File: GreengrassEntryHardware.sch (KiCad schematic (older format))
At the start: 29 parts

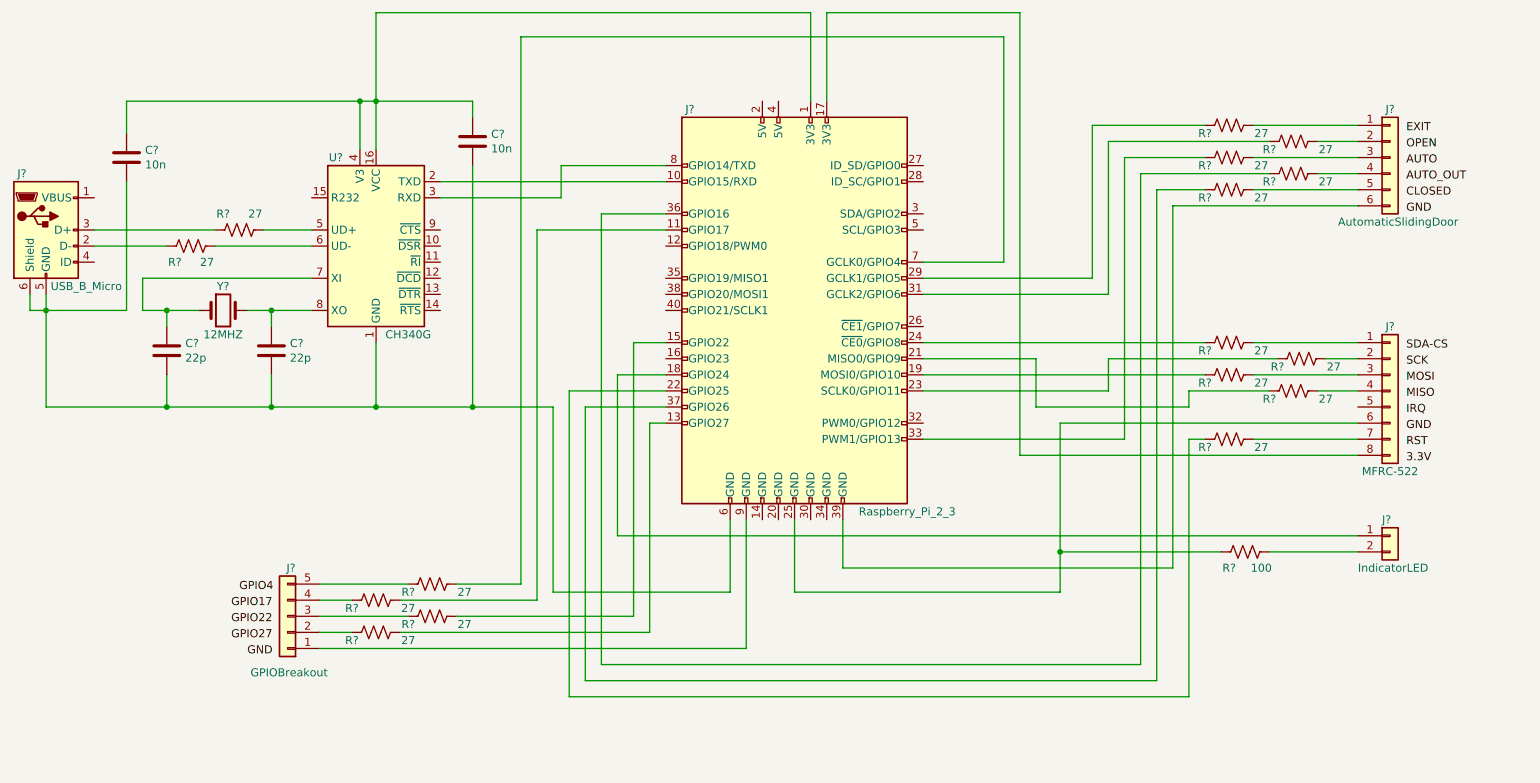
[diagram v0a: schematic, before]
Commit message: WIP: finished usb to uart design
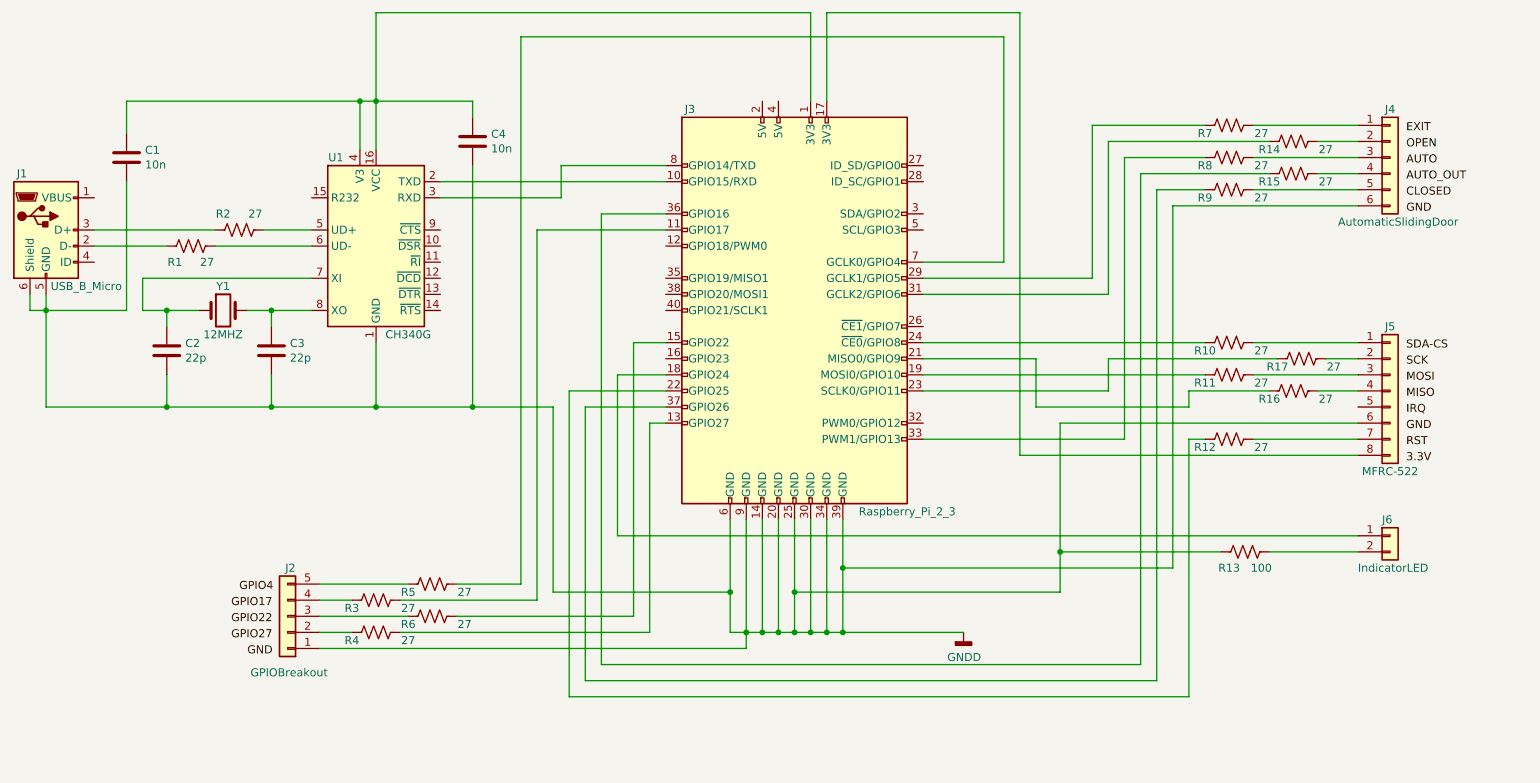
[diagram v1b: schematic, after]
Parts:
- C1, C2, C3, C4: renamed from C?; footprint (none) -> Capacitor_SMD:C_0805_2012Metric_Pad1.15x1.40mm_HandSolder
- J1: renamed from J?; footprint (none) -> GreengrassEntryHardware:MicroUSB
- J2: renamed from J?; footprint (none) -> Connector_PinHeader_2.54mm:PinHeader_1x05_P2.54mm_Vertical
- J3: renamed from J?; footprint (none) -> Connector_PinSocket_2.54mm:PinSocket_2x20_P2.54mm_Vertical
- J4: renamed from J?; footprint (none) -> Connector_PinHeader_2.54mm:PinHeader_1x06_P2.54mm_Vertical
- J5: renamed from J?; footprint (none) -> Connector_PinHeader_2.54mm:PinHeader_1x08_P2.54mm_Vertical
- J6: renamed from J?; footprint (none) -> Connector_PinHeader_2.54mm:PinHeader_2x01_P2.54mm_Horizontal
- R1, R10, R11, R12, R13, R14, R15, R16, R17, R2, R3, R4, R5, R6, R7, R8, R9: renamed from R?; footprint (none) -> Resistor_SMD:R_0805_2012Metric_Pad1.15x1.40mm_HandSolder
- Y1: renamed from Y?; footprint (none) -> Crystal:Crystal_SMD_HC49-SD_HandSoldering
- gave numbers to parts that had none: 1
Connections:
- net GNDD: now reaches J3.14 (GND)
- net GNDD: now also C1.2, C2.2, C3.2, C4.2, J1.5 (GND), J1.6 (Shield), J2.1 (Pin_1), J3.20 (GND), J3.25 (GND), J3.30 (GND), J3.34 (GND), J3.39 (GND), J3.6 (GND), J3.9 (GND), J4.6 (Pin_6), J5.6 (Pin_6), R13.2, U1.1 (GND)

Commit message: Added GPIO breakout to pcb
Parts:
- J2: footprint Connector_PinHeader_2.54mm:PinHeader_1x05_P2.54mm_Vertical -> Connector_PinHeader_2.54mm:PinHeader_1x05_P2.54mm_Horizontal
- renumbered R4 to R3, R6 to R4, R3 to R5, R5 to R6
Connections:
- net at J3.11 (GPIO17): now also R4.1; no longer R5.1
- net at J3.13 (GPIO27): now also R5.1; no longer R3.1
- net at J3.15 (GPIO22): now also R6.1; no longer R4.1
- net at J3.7 (GCLK0/GPIO4): now also R3.1; no longer R6.1
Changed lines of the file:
@@
 Wire Wire Line
 	3300 4450 3900 4450
-Wire Wire Line
-	4400 5600 5500 5600
-Wire Wire Line
-	5500 5600 5500 5150
 Connection ~ 3300 4450
 $Comp
@@
 F 0 "J2" H 2700 5450 50  0000 L CNN
 F 1 "GPIOBreakout" H 2500 6100 50  0000 L CNN
-F 2 "Connector_PinHeader_2.54mm:PinHeader_1x05_P2.54mm_Vertical" H 2750 5750 50  0001 C CNN
+F 2 "Connector_PinHeader_2.54mm:PinHeader_1x05_P2.54mm_Horizontal" H 2750 5750 50  0001 C CNN
 F 3 "~" H 2750 5750 50  0001 C CNN
 	1    2750 5750
@@
 Text Label 2500 6000 0    50   ~ 0
 GND
-Text Label 2450 5600 0    50   ~ 0
+Text Label 2450 5900 0    50   ~ 0
 GPIO4
+Text Label 2400 5800 0    50   ~ 0
+GPIO17
 Text Label 2400 5700 0    50   ~ 0
-GPIO17
-Text Label 2400 5900 0    50   ~ 0
 GPIO27
-Text Label 2400 5800 0    50   ~ 0
-GPIO22
 Wire Wire Line
 	5600 5150 5600 5850
 Wire Wire Line
-	3800 5750 4900 5750
-Wire Wire Line
-	4900 5750 4900 4050
-Wire Wire Line
 	4900 4050 5100 4050
 Wire Wire Line
-	5000 5850 5000 4550
-Wire Wire Line
 	5000 4550 5100 4550
 Wire Wire Line
-	4300 5650 4300 3350
-Wire Wire Line
 	4300 3350 5100 3350
 Wire Wire Line
-	3800 5550 4200 5550
-Wire Wire Line
-	4200 5550 4200 2150
-Wire Wire Line
 	7200 2150 7200 3550
 Wire Wire Line
@@
 	4200 2150 7200 2150
 $Comp
-L Device:R_US R5
-U 1 1 5D518DBE
-P 3650 5550
-F 0 "R5" V 3700 5400 50  0000 C CNN
-F 1 "27" V 3700 5750 50  0000 C CNN
-F 2 "Resistor_SMD:R_0805_2012Metric_Pad1.15x1.40mm_HandSolder" V 3690 5540 50  0001 C CNN
-F 3 "~" H 3650 5550 50  0001 C CNN
-	1    3650 5550
-	0    1    1    0
-$EndComp
-$Comp
-L Device:R_US R6
-U 1 1 5D5193C5
-P 3650 5750
-F 0 "R6" V 3700 5600 50  0000 C CNN
-F 1 "27" V 3700 5950 50  0000 C CNN
-F 2 "Resistor_SMD:R_0805_2012Metric_Pad1.15x1.40mm_HandSolder" V 3690 5740 50  0001 C CNN
-F 3 "~" H 3650 5750 50  0001 C CNN
-	1    3650 5750
-	0    1    1    0
-$EndComp
-$Comp
-L Device:R_US R4
+L Device:R_US R3
 U 1 1 5D519DE6
 P 3300 5850
-F 0 "R4" V 3350 5700 50  0000 C CNN
+F 0 "R3" V 3350 5700 50  0000 C CNN
 F 1 "27" V 3350 6050 50  0000 C CNN
 F 2 "Resistor_SMD:R_0805_2012Metric_Pad1.15x1.40mm_HandSolder" V 3340 5840 50  0001 C CNN
@@
 	0    1    1    0
 $EndComp
-$Comp
-L Device:R_US R3
-U 1 1 5D51ABA1
-P 3300 5650
-F 0 "R3" V 3350 5500 50  0000 C CNN
-F 1 "27" V 3350 5850 50  0000 C CNN
-F 2 "Resistor_SMD:R_0805_2012Metric_Pad1.15x1.40mm_HandSolder" V 3340 5640 50  0001 C CNN
-F 3 "~" H 3300 5650 50  0001 C CNN
-	1    3300 5650
-	0    1    1    0
-$EndComp
-Wire Wire Line
-	2950 5550 3500 5550
 Wire Wire Line
 	2950 5650 3150 5650
@@
 	2950 5850 3150 5850
 Wire Wire Line
-	2950 5950 5600 5950
-Wire Wire Line
-	3450 5850 5000 5850
-Wire Wire Line
-	3450 5650 4300 5650
-Wire Wire Line
 	4800 5250 4800 4250
 Wire Wire Line
@@
 	3700 3050 5100 3050
 Wire Wire Line
-	4400 4450 4400 5600
+	4400 4450 4400 5350
 Wire Wire Line
 	8450 4650 8350 4650
@@
 	9400 5250 4800 5250
 $Comp
-L power:GNDD #PWR?
+L power:GNDD #PWR0101
 U 1 1 5D3B21CF
 P 6950 5850
-F 0 "#PWR?" H 6950 5600 50  0001 C CNN
+F 0 "#PWR0101" H 6950 5600 50  0001 C CNN
 F 1 "GNDD" H 6954 5695 50  0000 C CNN
 F 2 "" H 6950 5850 50  0001 C CNN
@@
 	5600 5850 5600 5950
 Wire Wire Line
-	5500 5600 5500 5850
-Wire Wire Line
 	5500 5850 5600 5850
-Connection ~ 5500 5600
+Wire Wire Line
+	5500 5150 5500 5350
+Wire Wire Line
+	5500 5350 4400 5350
+Connection ~ 5500 5350
+Wire Wire Line
+	5000 4550 5000 5650
+Wire Wire Line
+	4900 4050 4900 5550
+Wire Wire Line
+	4300 3350 4300 5750
+Wire Wire Line
+	5500 5350 5500 5850
+Wire Wire Line
+	2950 5550 3500 5550
+Wire Wire Line
+	3450 5850 4200 5850
+Wire Wire Line
+	4200 2150 4200 5850
+Wire Wire Line
+	3800 5750 4300 5750
+Wire Wire Line
+	2950 5950 5600 5950
+Wire Wire Line
+	3450 5650 5000 5650
+Wire Wire Line
+	3800 5550 4900 5550
+$Comp
+L Device:R_US R6
+U 1 1 5D518DBE
+P 3650 5550
+F 0 "R6" V 3700 5400 50  0000 C CNN
+F 1 "27" V 3700 5750 50  0000 C CNN
+F 2 "Resistor_SMD:R_0805_2012Metric_Pad1.15x1.40mm_HandSolder" V 3690 5540 50  0001 C CNN
+F 3 "~" H 3650 5550 50  0001 C CNN
+	1    3650 5550
+	0    1    1    0
+$EndComp
+$Comp
+L Device:R_US R5
+U 1 1 5D51ABA1
+P 3300 5650
+F 0 "R5" V 3350 5500 50  0000 C CNN
+F 1 "27" V 3350 5850 50  0000 C CNN
+F 2 "Resistor_SMD:R_0805_2012Metric_Pad1.15x1.40mm_HandSolder" V 3340 5640 50  0001 C CNN
+F 3 "~" H 3300 5650 50  0001 C CNN
+	1    3300 5650
+	0    1    1    0
+$EndComp
+$Comp
+L Device:R_US R4
+U 1 1 5D5193C5
+P 3650 5750
+F 0 "R4" V 3700 5600 50  0000 C CNN
+F 1 "27" V 3700 5950 50  0000 C CNN
+F 2 "Resistor_SMD:R_0805_2012Metric_Pad1.15x1.40mm_HandSolder" V 3690 5740 50  0001 C CNN
+F 3 "~" H 3650 5750 50  0001 C CNN
+	1    3650 5750
+	0    1    1    0
+$EndComp
+Text Label 2400 5600 0    50   ~ 0
+GPIO22
 $EndSCHEMATC

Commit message: Tidied up the mfrc pcb layout
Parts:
- removed J6: IndicatorLED, Connector_PinHeader_2.54mm:PinHeader_2x01_P2.54mm_Horizontal, symbol Connector_Generic:Conn_01x02
- added R18: 27, Resistor_SMD:R_0805_2012Metric_Pad1.15x1.40mm_HandSolder, symbol Device:R_US
- J5: footprint Connector_PinHeader_2.54mm:PinHeader_1x08_P2.54mm_Vertical -> Connector_PinHeader_2.54mm:PinHeader_2x05_P2.54mm_Horizontal; symbol Connector_Generic:Conn_01x08 -> Connector_Generic:Conn_01x10
- R13: value 100 -> 27
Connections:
- net GNDD: now also J4.1 (Pin_1); no longer J4.6 (Pin_6), R13.2
- net at J3.16 (GPIO23): now also R18.2
- net at J3.18 (GPIO24): now also R13.2
- net at R7.1: now also J4.2 (Pin_2); no longer J4.1 (Pin_1)
- net at R14.1: now also J4.3 (Pin_3); no longer J4.2 (Pin_2)
- net at R8.1: now also J4.4 (Pin_4); no longer J4.3 (Pin_3)
- net at R15.1: now also J4.5 (Pin_5); no longer J4.4 (Pin_4)
- net at R9.1: now also J4.6 (Pin_6); no longer J4.5 (Pin_5)
- net at R13.1: now also J5.9 (Pin_9)
- new net: J5.10 (Pin_10), R18.1
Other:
- moved on the sheet: J4, R17
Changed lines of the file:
@@
 SDA-CS
 $Comp
-L Connector_Generic:Conn_01x08 J5
+L Connector_Generic:Conn_01x10 J5
 U 1 1 5D3BD9C3
-P 9600 4350
-F 0 "J5" H 9600 4750 50  0000 C CNN
+P 9600 4450
+F 0 "J5" H 9600 5000 50  0000 C CNN
 F 1 "MFRC-522" H 9600 3850 50  0000 C CNN
-F 2 "Connector_PinHeader_2.54mm:PinHeader_1x08_P2.54mm_Vertical" H 9600 4350 50  0001 C CNN
-F 3 "~" H 9600 4350 50  0001 C CNN
-	1    9600 4350
+F 2 "Connector_PinHeader_2.54mm:PinHeader_2x05_P2.54mm_Horizontal" H 9600 4450 50  0001 C CNN
+F 3 "~" H 9600 4450 50  0001 C CNN
+	1    9600 4450
 	1    0    0    -1
 $EndComp
@@
 Wire Wire Line
 	4500 4350 4500 6250
-Text Label 9700 3250 0    50   ~ 0
+Text Label 9700 2650 0    50   ~ 0
 GND
 Text Label 9700 3150 0    50   ~ 0
@@
 L Connector_Generic:Conn_01x06 J4
 U 1 1 5D3C1839
-P 9600 2900
-F 0 "J4" H 9600 3200 50  0000 C CNN
-F 1 "AutomaticSlidingDoor" H 9650 2500 50  0000 C CNN
-F 2 "Connector_PinHeader_2.54mm:PinHeader_1x06_P2.54mm_Vertical" H 9600 2900 50  0001 C CNN
-F 3 "~" H 9600 2900 50  0001 C CNN
-	1    9600 2900
+P 9600 2800
+F 0 "J4" H 9600 3100 50  0000 C CNN
+F 1 "AutomaticSlidingDoor" H 9650 2400 50  0000 C CNN
+F 2 "Connector_PinHeader_2.54mm:PinHeader_1x06_P2.54mm_Vertical" H 9600 2800 50  0001 C CNN
+F 3 "~" H 9600 2800 50  0001 C CNN
+	1    9600 2800
 	1    0    0    -1
 $EndComp
@@
 	6100 2000 7300 2000
 Wire Wire Line
-	8250 3200 8250 5450
-Wire Wire Line
 	7550 5600 5900 5600
 Wire Wire Line
 	5900 5600 5900 5150
-Wire Wire Line
-	6200 5150 6200 5450
-Wire Wire Line
-	6200 5450 8250 5450
 Wire Wire Line
 	8450 3100 8150 3100
@@
 	3300 4450 3900 4450
 Connection ~ 3300 4450
-$Comp
-L Connector_Generic:Conn_01x02 J6
-U 1 1 5D44B757
-P 9600 5250
-F 0 "J6" H 9550 5350 50  0000 L CNN
-F 1 "IndicatorLED" H 9400 5050 50  0000 L CNN
-F 2 "Connector_PinHeader_2.54mm:PinHeader_2x01_P2.54mm_Horizontal" H 9600 5250 50  0001 C CNN
-F 3 "~" H 9600 5250 50  0001 C CNN
-	1    9600 5250
-	1    0    0    -1
-$EndComp
 Wire Wire Line
 	4800 4250 5100 4250
@@
 L Device:R_US R17
 U 1 1 5D47C1CF
-P 9050 4150
-F 0 "R17" V 9100 4000 50  0000 C CNN
-F 1 "27" V 9100 4350 50  0000 C CNN
-F 2 "Resistor_SMD:R_0805_2012Metric_Pad1.15x1.40mm_HandSolder" V 9090 4140 50  0001 C CNN
-F 3 "~" H 9050 4150 50  0001 C CNN
-	1    9050 4150
-	0    1    1    0
-$EndComp
-Wire Wire Line
-	8900 4150 7850 4150
+P 9000 4150
+F 0 "R17" V 9050 4000 50  0000 C CNN
+F 1 "27" V 9050 4350 50  0000 C CNN
+F 2 "Resistor_SMD:R_0805_2012Metric_Pad1.15x1.40mm_HandSolder" V 9040 4140 50  0001 C CNN
+F 3 "~" H 9000 4150 50  0001 C CNN
+	1    9000 4150
+	0    1    1    0
+$EndComp
 $Comp
 L Device:R_US R11
@@
 	8750 3100 9400 3100
 Wire Wire Line
-	8250 3200 9400 3200
-Wire Wire Line
 	7850 2800 8850 2800
 Wire Wire Line
@@
 Wire Wire Line
 	8750 4050 9400 4050
-Wire Wire Line
-	9200 4150 9400 4150
 Wire Wire Line
 	8750 4250 9400 4250
@@
 	1150 3850 1250 3850
 $Comp
-L Device:R_US R13
-U 1 1 5D455FFA
-P 8700 5350
-F 0 "R13" V 8800 5250 50  0000 C CNN
-F 1 "100" V 8800 5450 50  0000 C CNN
-F 2 "Resistor_SMD:R_0805_2012Metric_Pad1.15x1.40mm_HandSolder" V 8740 5340 50  0001 C CNN
-F 3 "~" H 8700 5350 50  0001 C CNN
-	1    8700 5350
-	0    1    1    0
-$EndComp
-Wire Wire Line
-	7550 4550 7550 5350
-Wire Wire Line
-	8550 5350 7550 5350
-Connection ~ 7550 5350
-Wire Wire Line
-	7550 5350 7550 5600
-Wire Wire Line
-	8850 5350 9400 5350
-Wire Wire Line
-	9400 5250 4800 5250
-$Comp
 L power:GNDD #PWR0101
 U 1 1 5D3B21CF
@@
 	6950 5850 6200 5850
 Wire Wire Line
-	6200 5850 6200 5450
-Connection ~ 6200 5450
-Wire Wire Line
 	6200 5850 6100 5850
 Wire Wire Line
@@
 	5500 5850 5600 5850
 Wire Wire Line
-	5500 5150 5500 5350
-Wire Wire Line
-	5500 5350 4400 5350
-Connection ~ 5500 5350
-Wire Wire Line
 	5000 4550 5000 5650
 Wire Wire Line
@@
 Wire Wire Line
 	4300 3350 4300 5750
-Wire Wire Line
-	5500 5350 5500 5850
 Wire Wire Line
 	2950 5550 3500 5550
@@
 Text Label 2400 5600 0    50   ~ 0
 GPIO22
+Text Label 9700 4900 0    50   ~ 0
+LED
+$Comp
+L Device:R_US R13
+U 1 1 5D59BAAD
+P 8600 4850
+F 0 "R13" V 8650 4700 50  0000 C CNN
+F 1 "27" V 8650 5050 50  0000 C CNN
+F 2 "Resistor_SMD:R_0805_2012Metric_Pad1.15x1.40mm_HandSolder" V 8640 4840 50  0001 C CNN
+F 3 "~" H 8600 4850 50  0001 C CNN
+	1    8600 4850
+	0    1    1    0
+$EndComp
+Wire Wire Line
+	7950 4850 7950 5250
+Wire Wire Line
+	7950 5250 4800 5250
+Wire Wire Line
+	7550 4550 7550 5600
+Wire Wire Line
+	5500 5350 5500 5850
+Wire Wire Line
+	5500 5150 5500 5350
+Connection ~ 5500 5350
+Wire Wire Line
+	5500 5350 4400 5350
+Wire Wire Line
+	6200 5150 6200 5350
+Wire Wire Line
+	6200 5350 7650 5350
+Connection ~ 6200 5350
+Wire Wire Line
+	6200 5350 6200 5850
+Wire Wire Line
+	8750 4850 9400 4850
+Wire Wire Line
+	7950 4850 8450 4850
+$Comp
+L Device:R_US R18
+U 1 1 5D61EB3A
+P 9000 4950
+F 0 "R18" V 9050 4800 50  0000 C CNN
+F 1 "27" V 9050 5150 50  0000 C CNN
+F 2 "Resistor_SMD:R_0805_2012Metric_Pad1.15x1.40mm_HandSolder" V 9040 4940 50  0001 C CNN
+F 3 "~" H 9000 4950 50  0001 C CNN
+	1    9000 4950
+	0    1    1    0
+$EndComp
+Wire Wire Line
+	9150 4150 9400 4150
+Wire Wire Line
+	8850 4150 7850 4150
+Wire Wire Line
+	9150 4950 9400 4950
+Wire Wire Line
+	8850 4950 8450 4950
+Wire Wire Line
+	8450 4950 8450 5450
+Wire Wire Line
+	8450 5450 4100 5450
+Wire Wire Line
+	4100 5450 4100 4150
+Wire Wire Line
+	4100 4150 5100 4150
+Text Label 9700 5000 0    50   ~ 0
+BUZZER
+Wire Wire Line
+	7650 2600 7650 5350
+Wire Wire Line
+	7650 2600 9400 2600
 $EndSCHEMATC

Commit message: Added the door connector to the pcb
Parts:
- J4: footprint Connector_PinHeader_2.54mm:PinHeader_1x06_P2.54mm_Vertical -> Connector_PinHeader_2.54mm:PinHeader_1x06_P2.54mm_Horizontal
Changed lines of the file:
@@
 F 0 "J4" H 9600 3100 50  0000 C CNN
 F 1 "AutomaticSlidingDoor" H 9650 2400 50  0000 C CNN
-F 2 "Connector_PinHeader_2.54mm:PinHeader_1x06_P2.54mm_Vertical" H 9600 2800 50  0001 C CNN
+F 2 "Connector_PinHeader_2.54mm:PinHeader_1x06_P2.54mm_Horizontal" H 9600 2800 50  0001 C CNN
 F 3 "~" H 9600 2800 50  0001 C CNN
 	1    9600 2800

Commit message: Update schematic and pcb to use Molex SPOX connector for the automatic door
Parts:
- J4: footprint Connector_PinHeader_2.54mm:PinHeader_1x06_P2.54mm_Horizontal -> GreengrassEntryHardware:Molex_SPOX_5267-06A_1x06_P2.50mm_Horizontal
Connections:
- net at J3.29 (GCLK1/GPIO5): now also R9.2; no longer R7.2
- net at J3.31 (GCLK2/GPIO6): now also R15.2; no longer R14.2
- net at J3.36 (GPIO16): now also R14.2; no longer R15.2
- net at J3.37 (GPIO26): now also R7.2; no longer R9.2
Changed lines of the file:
@@
 F 0 "J4" H 9600 3100 50  0000 C CNN
 F 1 "AutomaticSlidingDoor" H 9650 2400 50  0000 C CNN
-F 2 "Connector_PinHeader_2.54mm:PinHeader_1x06_P2.54mm_Horizontal" H 9600 2800 50  0001 C CNN
+F 2 "GreengrassEntryHardware:Molex_SPOX_5267-06A_1x06_P2.50mm_Horizontal" H 9600 2800 50  0001 C CNN
 F 3 "~" H 9600 2800 50  0001 C CNN
 	1    9600 2800
@@
 	5900 5600 5900 5150
 Wire Wire Line
-	8450 3100 8150 3100
-Wire Wire Line
-	8150 3100 8150 6150
-Wire Wire Line
 	8150 6150 4600 6150
 Wire Wire Line
@@
 	4600 4450 5100 4450
 Wire Wire Line
-	8450 2900 7950 2900
-Wire Wire Line
-	7950 2900 7950 4650
-Wire Wire Line
 	7950 4650 6700 4650
 Wire Wire Line
-	7850 2800 7850 3750
-Wire Wire Line
 	7850 3750 6700 3750
-Wire Wire Line
-	8450 2700 7750 2700
-Wire Wire Line
-	7750 2700 7750 3650
 Wire Wire Line
 	7750 3650 6700 3650
@@
 	8750 3100 9400 3100
 Wire Wire Line
-	7850 2800 8850 2800
-Wire Wire Line
 	9400 2900 8750 2900
 Wire Wire Line
-	8050 3000 8850 3000
-Wire Wire Line
 	8750 4050 9400 4050
 Wire Wire Line
@@
 Wire Wire Line
 	9400 4750 7300 4750
-Wire Wire Line
-	8050 3000 8050 6050
 Wire Wire Line
 	4700 3250 4700 6050
@@
 BUZZER
 Wire Wire Line
+	7650 2600 9400 2600
+Wire Wire Line
 	7650 2600 7650 5350
 Wire Wire Line
-	7650 2600 9400 2600
+	8150 6150 8150 2700
+Wire Wire Line
+	8150 2700 8450 2700
+Wire Wire Line
+	8850 2800 8050 2800
+Wire Wire Line
+	8050 2800 8050 6050
+Wire Wire Line
+	8450 2900 7950 2900
+Wire Wire Line
+	7950 2900 7950 4650
+Wire Wire Line
+	8850 3000 7850 3000
+Wire Wire Line
+	7850 3000 7850 3750
+Wire Wire Line
+	8450 3100 7750 3100
+Wire Wire Line
+	7750 3100 7750 3650
 $EndSCHEMATC
